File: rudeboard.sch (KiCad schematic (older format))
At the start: 147 parts, among them J1 Conn_01x04, J2 USB_B_Mini, SW1 SW_Push, U1 ATmega32U4-AU, Y1 16MHz

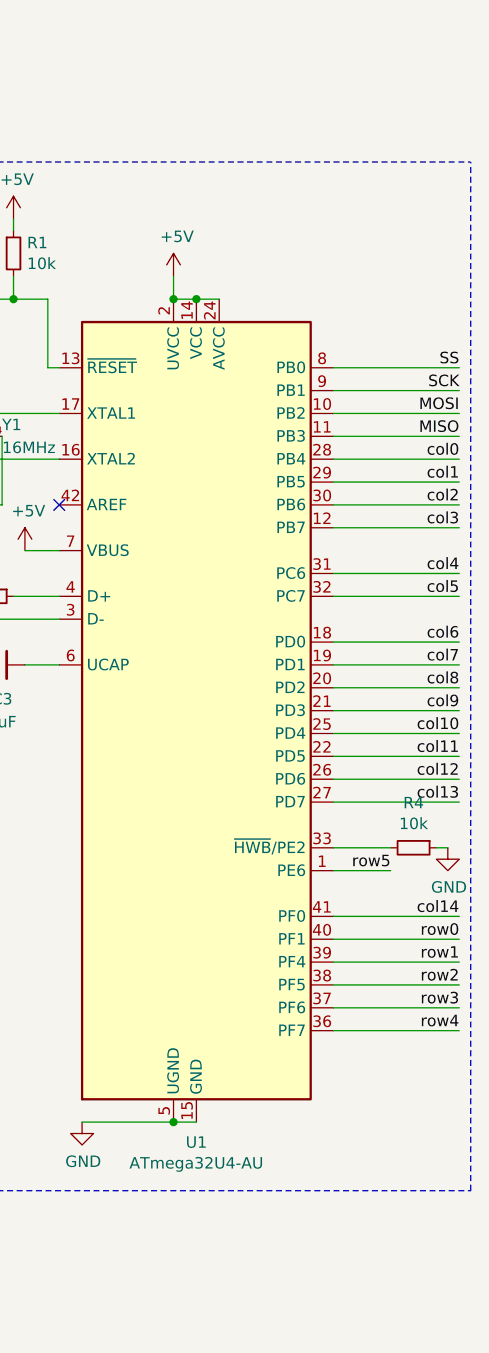
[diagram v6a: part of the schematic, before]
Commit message: route pcb for integrated mcu
- includes spi pin breakout
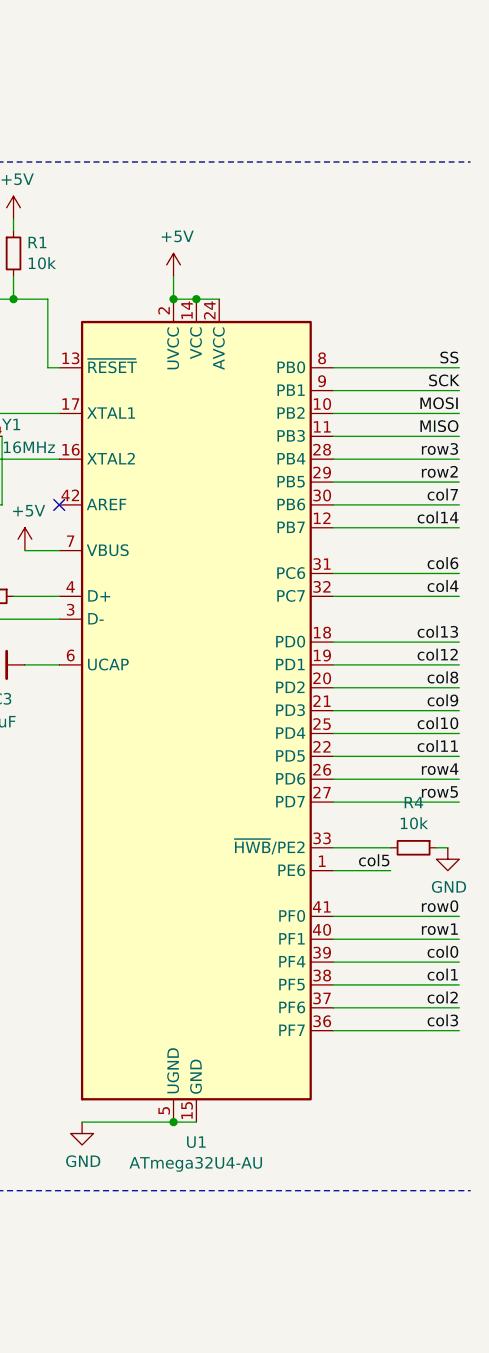
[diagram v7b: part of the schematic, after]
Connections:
- net col0: now also U1.39 (PF4); no longer U1.28 (PB4)
- net col1: now also U1.38 (PF5); no longer U1.29 (PB5)
- net col12: now also U1.19 (PD1); no longer U1.26 (PD6)
- net col13: now also U1.18 (PD0); no longer U1.27 (PD7)
- net col14: now also U1.12 (PB7); no longer U1.41 (PF0)
- net col2: now also U1.37 (PF6); no longer U1.30 (PB6)
- net col3: now also U1.36 (PF7); no longer U1.12 (PB7)
- net col4: now also U1.32 (PC7); no longer U1.31 (PC6)
- net col5: now also U1.1 (PE6); no longer U1.32 (PC7)
- net col6: now also U1.31 (PC6); no longer U1.18 (PD0)
- net col7: now also U1.30 (PB6); no longer U1.19 (PD1)
- net row0: now also U1.41 (PF0); no longer U1.40 (PF1)
- net row1: now also U1.40 (PF1); no longer U1.39 (PF4)
- net row2: now also U1.29 (PB5); no longer U1.38 (PF5)
- net row3: now also U1.28 (PB4); no longer U1.37 (PF6)
- net row4: now also U1.26 (PD6); no longer U1.36 (PF7)
- net row5: now also U1.27 (PD7); no longer U1.1 (PE6)
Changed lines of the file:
@@
 Wire Wire Line
 	9200 1600 9200 1650
-Wire Wire Line
-	10600 2550 11150 2550
-Text Label 11150 2550 2    50   ~ 0
-MISO
-Wire Wire Line
-	10600 2450 11150 2450
 Text Label 11150 2450 2    50   ~ 0
 MOSI
-Wire Wire Line
-	10600 2350 11150 2350
 Text Label 11150 2350 2    50   ~ 0
 SCK
-Wire Wire Line
-	10600 2250 11150 2250
 Text Label 11150 2250 2    50   ~ 0
 SS
@@
 	8500 5850 11200 5850
 Wire Notes Line
-	11200 5850 11200 1350
-Wire Notes Line
 	8500 1350 11200 1350
 Text Notes 8500 1300 0    50   ~ 0
@@
 	10600 2650 11150 2650
 Wire Wire Line
-	10600 2750 11150 2750
-Wire Wire Line
 	10600 2850 11150 2850
 Wire Wire Line
@@
 	10600 4050 11150 4050
 Wire Wire Line
-	10600 3450 11150 3450
-Wire Wire Line
-	10600 3550 11150 3550
-Wire Wire Line
 	10600 3750 11150 3750
 Wire Wire Line
@@
 Wire Wire Line
 	10600 5150 11150 5150
-Text Label 11150 2650 2    50   ~ 0
-col0
-Text Label 11150 2750 2    50   ~ 0
-col1
+Text Label 11150 5150 2    50   ~ 0
+col3
+Text Label 11150 3250 2    50   ~ 0
+col4
+Text Label 10850 4450 2    50   ~ 0
+col5
+Text Label 11150 3150 2    50   ~ 0
+col6
 Text Label 11150 2850 2    50   ~ 0
-col2
-Text Label 11150 2950 2    50   ~ 0
-col3
-Text Label 11150 3150 2    50   ~ 0
-col4
-Text Label 11150 3250 2    50   ~ 0
-col5
-Text Label 11150 3450 2    50   ~ 0
-col6
-Text Label 11150 3550 2    50   ~ 0
 col7
 Text Label 11150 3650 2    50   ~ 0
@@
 Text Label 11150 3950 2    50   ~ 0
 col11
+Text Label 11150 3550 2    50   ~ 0
+col12
+Text Label 11150 4650 2    50   ~ 0
+row0
+Text Label 11150 2750 2    50   ~ 0
+row2
+Text Label 11150 2650 2    50   ~ 0
+row3
 Text Label 11150 4050 2    50   ~ 0
-col12
+row4
 Text Label 11150 4150 2    50   ~ 0
-col13
-Text Label 11150 4650 2    50   ~ 0
-col14
-Text Label 11150 4750 2    50   ~ 0
-row0
-Text Label 11150 4850 2    50   ~ 0
-row1
-Text Label 11150 4950 2    50   ~ 0
-row2
-Text Label 11150 5050 2    50   ~ 0
-row3
-Text Label 11150 5150 2    50   ~ 0
-row4
-Text Label 10850 4450 2    50   ~ 0
 row5
 Wire Wire Line
@@
 	1    0    0    -1
 $EndComp
+Text Label 11150 4850 2    50   ~ 0
+col0
+Text Label 11150 4950 2    50   ~ 0
+col1
+Text Label 11150 5050 2    50   ~ 0
+col2
+Wire Wire Line
+	10600 2750 11150 2750
+Text Label 11150 2950 2    50   ~ 0
+col14
+Text Label 11150 3450 2    50   ~ 0
+col13
+Text Label 11150 4750 2    50   ~ 0
+row1
+Text Label 11150 2550 2    50   ~ 0
+MISO
+Wire Wire Line
+	10600 2550 11150 2550
+Wire Wire Line
+	10600 2450 11150 2450
+Wire Wire Line
+	10600 2350 11150 2350
+Wire Wire Line
+	10600 2250 11150 2250
+Wire Wire Line
+	10600 3450 11150 3450
+Wire Wire Line
+	10600 3550 11150 3550
 $EndSCHEMATC
